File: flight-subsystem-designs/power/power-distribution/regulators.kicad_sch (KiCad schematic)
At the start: 43 parts, among them U6 LT8610, U7 LT8610, U8 LT8610

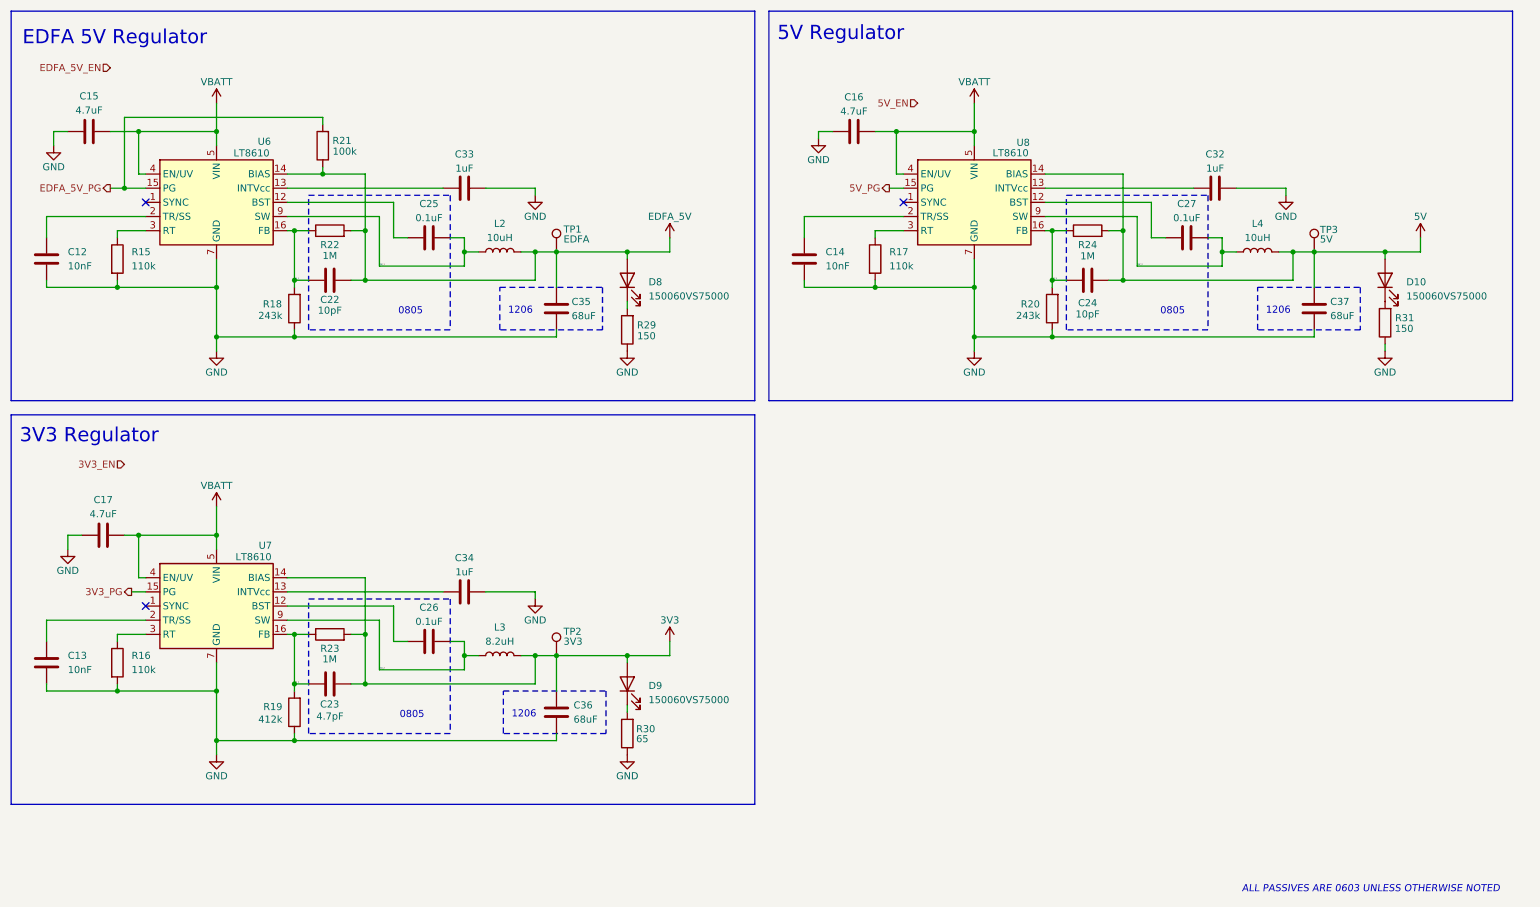
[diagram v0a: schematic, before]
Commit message: feat: PDU 4.0.0 (WIP)
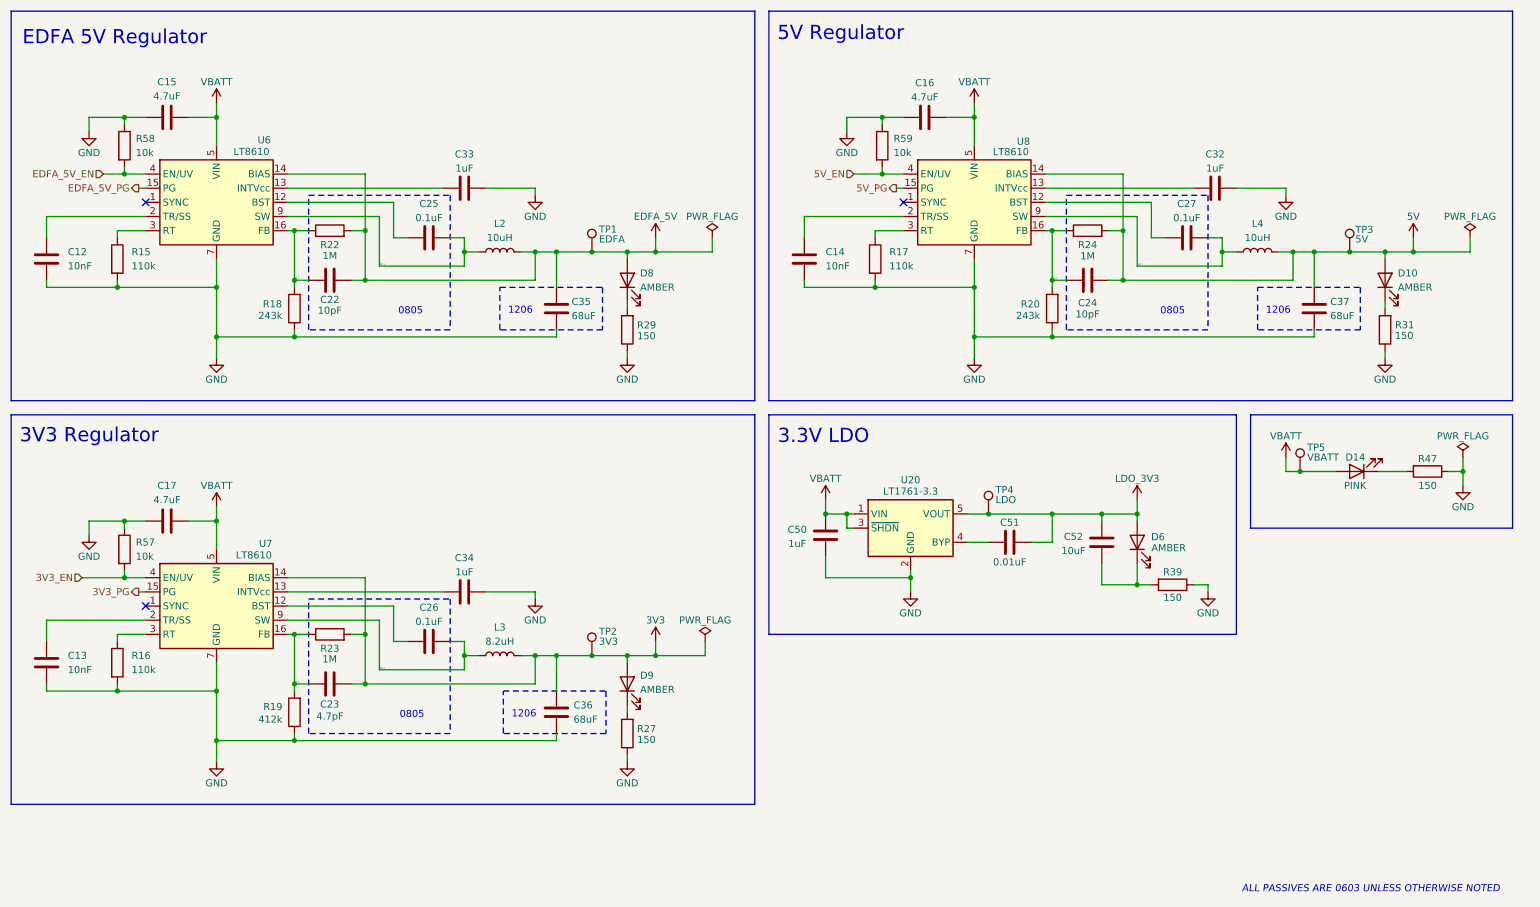
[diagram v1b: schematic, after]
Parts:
- removed R21: 100k, Resistor_SMD:R_0603_1608Metric, symbol Device:R
- removed R30: 65, Resistor_SMD:R_0603_1608Metric, symbol Device:R
- added C50: 1uF, Capacitor_SMD:C_0603_1608Metric, symbol Device:C
- added C51: 0.01uF, Capacitor_SMD:C_0603_1608Metric, symbol Device:C
- added C52: 10uF, Capacitor_SMD:C_0603_1608Metric, symbol Device:C
- added D14: PINK, LED_SMD:LED_0603_1608Metric, symbol Device:LED
- added D6: AMBER, LED_SMD:LED_0603_1608Metric, symbol Device:LED
- added R27, R39, R47: 150, Resistor_SMD:R_0603_1608Metric, symbol Device:R
- added R57, R58, R59: 10k, Resistor_SMD:R_0603_1608Metric, symbol Device:R
- added TP4: LDO, TestPoint:TestPoint_Keystone_5000-5004_Miniature, symbol Connector:TestPoint
- added TP5: VBATT, TestPoint:TestPoint_Keystone_5000-5004_Miniature, symbol Connector:TestPoint
- added U20: LT1761-3.3, Package_TO_SOT_SMD:TSOT-23-5, symbol Regulator_Linear:LT1761-2
- C37: footprint Capacitor_SMD:C_0805_2012Metric -> Capacitor_SMD:C_1206_3216Metric
- D10, D8, D9: value 150060VS75000 -> AMBER
- R31: footprint Capacitor_SMD:C_1206_3216Metric -> Resistor_SMD:R_0603_1608Metric
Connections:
- net 3V3_EN: now also U7.4 (EN/UV), R57.2
- net 5V_EN: now also U8.4 (EN/UV), R59.2
- net EDFA_5V_EN: now also U6.4 (EN/UV), R58.2
- net GND: now also C50.1, R27.1, R39.1, R47.1, R57.1, R58.1, R59.1, U20.2 (GND)
- net VBATT: now also C50.2, D14.2 (A), TP5.1, U20.1 (VIN), U20.3 (~{SHDN}); no longer U6.4 (EN/UV), U7.4 (EN/UV), U8.4 (EN/UV)
- net at D9.1 (K): now also R27.2
- new net: D14.1 (K), R47.2
- new net: C52.1, D6.1 (K), R39.2
- new net: C51.2, U20.4 (BYP)
- new net LDO_3V3: C51.1, C52.2, D6.2 (A), TP4.1, U20.5 (VOUT)
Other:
- note added: "3.3V LDO"
- moved on the sheet: C15, C16, C17, R31, TP1, TP2, TP3
